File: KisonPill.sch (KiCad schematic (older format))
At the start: 44 parts, among them J1 USB_C_Receptacle_USB2.0, J2 Conn_01x17_Male, J3 Conn_01x17_Male, J4 Conn_01x03_Male, J5 Conn_01x04_Male, J6 Conn_01x03_Male, J7 Conn_01x08_Male, Q1 2N3904S-RTK/PS, Q2 2N3904S-RTK/PS, SW1 SW_Push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

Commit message: save
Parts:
- removed U4: ESP32JtagConnector, KisonCommon:jtag1.27, symbol KisonCommon:ESP32JtagConnector
- added R14, R15: 0, Resistor_SMD:R_0603_1608Metric, symbol Device:R
- added U4: ESP32FullConnector-KisonCommon, KisonCommon:jtag1.27-12, symbol KisonPill-rescue:ESP32FullConnector-KisonCommon
- added U7: ESP32FullConnector, Connector_Molex:Molex_CLIK-Mate_502382-1270_1x12-1MP_P1.25mm_Vertical, symbol KisonPill-rescue:ESP32FullConnector-KisonCommon
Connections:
- net +3V3: now also U4.7 (3V3), U7.7 (3V3)
- net DTR: now also Q2.1 (E); no longer Q2.3 (C)
- net EN: now also U4.1 (TRST), U7.1 (TRST)
- net EXT_5V: now also U4.8 (5V), U7.8 (5V)
- net GND: now also U4.2 (GND), U7.2 (GND)
- net IO0: now also Q2.3 (C), U4.12 (IO0), U7.12 (IO0); no longer Q2.1 (E)
- net IO12: now also U4.3 (TDI), U7.3 (TDI)
- net IO13: now also U4.4 (TCLK), U7.4 (TCLK)
- net IO14: now also U4.5 (TMS), U7.5 (TMS)
- net IO15: now also U4.6 (TDO), U7.6 (TDO); no longer J7.6 (Pin_6)
- net IO32: now also J7.6 (Pin_6)
- net RXD0: now also R14.2, U7.10 (RX)
- net TXD0: now also R15.1, U7.9 (TX)
- new net: R14.1, U4.10 (RX)
- new net: R15.2, U4.9 (TX)
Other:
- note added: "Should we isolate IO0 and rx,tx from Connector to on board?"
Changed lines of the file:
@@
 F 4 "C18536" H 3000 1300 50  0001 C CNN "LCSC"
 	1    3000 1300
-	1    0    0    -1
+	1    0    0    1
 $EndComp
 Wire Wire Line
@@
 Text Label 3100 550  0    50   ~ 0
 EN
-$Comp
-L KisonCommon:ESP32JtagConnector U4
-U 1 1 605BFB02
-P 6750 650
-F 0 "U4" H 6760 775 50  0000 C CNN
-F 1 "ESP32JtagConnector" H 6760 684 50  0000 C CNN
-F 2 "KisonCommon:jtag1.27" H 6750 650 50  0001 C CNN
-F 3 "" H 6750 650 50  0001 C CNN
-	1    6750 650
-	1    0    0    -1
-$EndComp
 $Comp
 L power:+3.3V #PWR012
@@
 Text Label 9250 1600 0    50   ~ 0
 TXD0
-$Comp
-L power:GND #PWR011
-U 1 1 60603F1F
-P 6550 750
-F 0 "#PWR011" H 6550 500 50  0001 C CNN
-F 1 "GND" V 6555 622 50  0000 R CNN
-F 2 "" H 6550 750 50  0001 C CNN
-F 3 "" H 6550 750 50  0001 C CNN
-	1    6550 750
-	0    1    1    0
-$EndComp
-Text Label 7050 750  0    50   ~ 0
+Text Label 5760 910  0    50   ~ 0
 EN
-Wire Wire Line
-	6970 750  7050 750
-Text Label 7050 820  0    50   ~ 0
+Text Label 5760 980  0    50   ~ 0
 IO12
-Wire Wire Line
-	6970 820  7050 820
-Text Label 7050 880  0    50   ~ 0
+Text Label 5760 1050 0    50   ~ 0
 IO14
-Wire Wire Line
-	6970 880  7050 880
-Text Label 6440 820  3    50   ~ 0
-IO13
-Wire Wire Line
-	6440 820  6550 820
-Text Label 6550 880  3    50   ~ 0
-IO15
 $Comp
 L Regulator_Linear:AZ1117-3.3 U3
@@
 Text Label 10220 4300 0    50   ~ 0
 IO4
-Text Label 10220 4400 0    50   ~ 0
-IO15
 Text Label 10220 4500 0    50   ~ 0
 IO5
 Text Label 10220 4600 0    50   ~ 0
 IO35
+Text Label 10220 4400 0    50   ~ 0
+IO32
+$Comp
+L power:+3V3 #PWR0124
+U 1 1 6059C21E
+P 6040 1120
+F 0 "#PWR0124" H 6040 970 50  0001 C CNN
+F 1 "+3V3" H 6055 1293 50  0000 C CNN
+F 2 "" H 6040 1120 50  0001 C CNN
+F 3 "" H 6040 1120 50  0001 C CNN
+	1    6040 1120
+	1    0    0    -1
+$EndComp
+Wire Wire Line
+	6040 1120 5760 1120
+$Comp
+L Device:R R15
+U 1 1 605D512D
+P 5910 1190
+F 0 "R15" V 5910 1190 50  0000 C CNN
+F 1 "0" V 5990 1190 50  0000 C CNN
+F 2 "Resistor_SMD:R_0603_1608Metric" V 5840 1190 50  0001 C CNN
+F 3 "~" H 5910 1190 50  0001 C CNN
+	1    5910 1190
+	0    1    1    0
+$EndComp
+Text Label 6060 1190 0    50   ~ 0
+TXD0
+$Comp
+L KisonPill-rescue:ESP32FullConnector-KisonCommon U7
+U 1 1 605F623D
+P 5750 1880
+F 0 "U7" H 5560 2304 50  0000 C CNN
+F 1 "ESP32FullConnector" H 5560 2213 50  0000 C CNN
+F 2 "Connector_Molex:Molex_CLIK-Mate_502382-1270_1x12-1MP_P1.25mm_Vertical" H 5750 1880 50  0001 C CNN
+F 3 "" H 5750 1880 50  0001 C CNN
+	1    5750 1880
+	1    0    0    -1
+$EndComp
+$Comp
+L power:GND #PWR011
+U 1 1 60603F1F
+P 5120 910
+F 0 "#PWR011" H 5120 660 50  0001 C CNN
+F 1 "GND" V 5125 782 50  0000 R CNN
+F 2 "" H 5120 910 50  0001 C CNN
+F 3 "" H 5120 910 50  0001 C CNN
+	1    5120 910
+	-1   0    0    1
+$EndComp
+Text Label 5340 980  2    50   ~ 0
+IO13
+Text Label 5340 1050 2    50   ~ 0
+IO15
+Wire Wire Line
+	5120 910  5340 910
+Text Label 5340 1120 2    50   ~ 0
+EXT_5V
+Text Label 5340 1260 3    50   ~ 0
+IO0
+$Comp
+L Device:R R14
+U 1 1 605CA1B8
+P 5190 1190
+F 0 "R14" V 5190 1190 50  0000 C CNN
+F 1 "0" V 5270 1190 50  0000 C CNN
+F 2 "Resistor_SMD:R_0603_1608Metric" V 5120 1190 50  0001 C CNN
+F 3 "~" H 5190 1190 50  0001 C CNN
+	1    5190 1190
+	0    1    1    0
+$EndComp
+Text Label 5040 1190 2    50   ~ 0
+RXD0
+$Comp
+L KisonPill-rescue:ESP32FullConnector-KisonCommon U4
+U 1 1 60586A77
+P 5740 1120
+F 0 "U4" H 5550 1544 50  0000 C CNN
+F 1 "ESP32FullConnector-KisonCommon" H 5550 1453 50  0000 C CNN
+F 2 "KisonCommon:jtag1.27-12" H 5740 1120 50  0001 C CNN
+F 3 "" H 5740 1120 50  0001 C CNN
+	1    5740 1120
+	1    0    0    -1
+$EndComp
+$Comp
+L power:GND #PWR09
+U 1 1 6060CCF1
+P 5130 1670
+F 0 "#PWR09" H 5130 1420 50  0001 C CNN
+F 1 "GND" V 5135 1542 50  0000 R CNN
+F 2 "" H 5130 1670 50  0001 C CNN
+F 3 "" H 5130 1670 50  0001 C CNN
+	1    5130 1670
+	-1   0    0    1
+$EndComp
+Text Label 5350 1740 2    50   ~ 0
+IO13
+Text Label 5350 1810 2    50   ~ 0
+IO15
+Wire Wire Line
+	5130 1670 5350 1670
+Text Label 5350 1880 2    50   ~ 0
+EXT_5V
+Text Label 5350 2020 3    50   ~ 0
+IO0
+Text Label 5770 1670 0    50   ~ 0
+EN
+Text Label 5770 1740 0    50   ~ 0
+IO12
+Text Label 5770 1810 0    50   ~ 0
+IO14
+$Comp
+L power:+3V3 #PWR010
+U 1 1 6061353C
+P 6050 1880
+F 0 "#PWR010" H 6050 1730 50  0001 C CNN
+F 1 "+3V3" H 6065 2053 50  0000 C CNN
+F 2 "" H 6050 1880 50  0001 C CNN
+F 3 "" H 6050 1880 50  0001 C CNN
+	1    6050 1880
+	1    0    0    -1
+$EndComp
+Wire Wire Line
+	6050 1880 5770 1880
+Wire Wire Line
+	5350 1950 5040 1950
+Wire Wire Line
+	5040 1950 5040 1190
+Wire Wire Line
+	5770 1950 6170 1950
+Wire Wire Line
+	6170 1950 6170 1190
+Wire Wire Line
+	6170 1190 6060 1190
+Text Notes 4400 610  0    50   ~ 0
+Should we isolate IO0 and rx,tx from Connector to on board?
 $EndSCHEMATC

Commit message: V1
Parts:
- removed C10, C9: 0.1uf, Capacitor_SMD:C_0603_1608Metric, symbol Device:C
- removed C8: 10uf, Capacitor_SMD:C_1206_3216Metric, symbol Device:C
- removed J2, J3: Conn_01x17_Male, Connector_PinHeader_2.54mm:PinHeader_1x17_P2.54mm_Vertical, symbol Connector:Conn_01x17_Male
- removed J4, J6: Conn_01x03_Male, Connector_PinHeader_2.54mm:PinHeader_1x03_P2.54mm_Vertical, symbol Connector:Conn_01x03_Male
- removed J5: Conn_01x04_Male, Connector_PinHeader_2.54mm:PinHeader_1x04_P2.54mm_Vertical, symbol Connector:Conn_01x04_Male
- removed J7: Conn_01x08_Male, Connector_PinHeader_2.54mm:PinHeader_1x08_P2.54mm_Vertical, symbol Connector:Conn_01x08_Male
- removed U5: ICM-20602, Package_LGA:LGA-16_3x3mm_P0.5mm_LayoutBorder3x5y, symbol Sensor_Motion:ICM-20602
- added J2, J3: Conn_01x19_Male, Connector_PinHeader_2.54mm:PinHeader_1x19_P2.54mm_Vertical, symbol Connector:Conn_01x19_Male
- U4, U7: symbol KisonPill-rescue:ESP32FullConnector-KisonCommon -> KisonCommon:ESP32FullConnector
- U6: footprint KisonCommon:USBLC6-2P6 -> KisonCommon:USBLC6-2P6-SOT666
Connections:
- net +3V3: now also J2.1 (Pin_1)
- net CLK: now also J3.19 (Pin_19)
- net CMD: now also J2.18 (Pin_18)
- net EN: now also J2.2 (Pin_2)
- net EXT_5V: now also J2.19 (Pin_19); no longer U4.8 (5V), U7.8 (5V)
- net GND: now also J2.14 (Pin_14), J3.1 (Pin_1), J3.7 (Pin_7)
- net IO0: now also J3.14 (Pin_14)
- net IO12: now also J2.13 (Pin_13)
- net IO13: now also J2.15 (Pin_15)
- net IO14: now also J2.12 (Pin_12)
- net IO15: now also J3.16 (Pin_16)
- net IO16: now also J3.12 (Pin_12)
- net IO17: now also J3.11 (Pin_11)
- net IO18: now also J3.9 (Pin_9)
- net IO19: now also J3.8 (Pin_8)
- net IO2: now also J3.15 (Pin_15)
- net IO21: now also J3.6 (Pin_6)
- net IO22: now also J3.3 (Pin_3)
- net IO23: now also J3.2 (Pin_2)
- net IO25: now also J2.9 (Pin_9)
- net IO26: now also J2.10 (Pin_10)
- net IO27: now also J2.11 (Pin_11)
- net IO32: now also J2.7 (Pin_7)
- net IO33: now also J2.8 (Pin_8)
- net IO34: now also J2.5 (Pin_5)
- net IO35: now also J2.6 (Pin_6)
- net IO4: now also J3.13 (Pin_13)
- net IO5: now also J3.10 (Pin_10)
- net RXD0: now also J3.5 (Pin_5); no longer U7.10 (RX)
- net SD0: now also J3.18 (Pin_18)
- net SD1: now also J3.17 (Pin_17)
- net SD2: now also J2.16 (Pin_16)
- net SD3: now also J2.17 (Pin_17)
- net SENSOR_VN: now also J2.4 (Pin_4)
- net SENSOR_VP: now also J2.3 (Pin_3)
- net TXD0: now also J3.4 (Pin_4); no longer U7.9 (TX)
- net at R14.1, U4.10 (RX): now also U7.10 (RX)
- net at R15.2, U4.9 (TX): now also U7.9 (TX)
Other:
- moved on the sheet: R14, R15

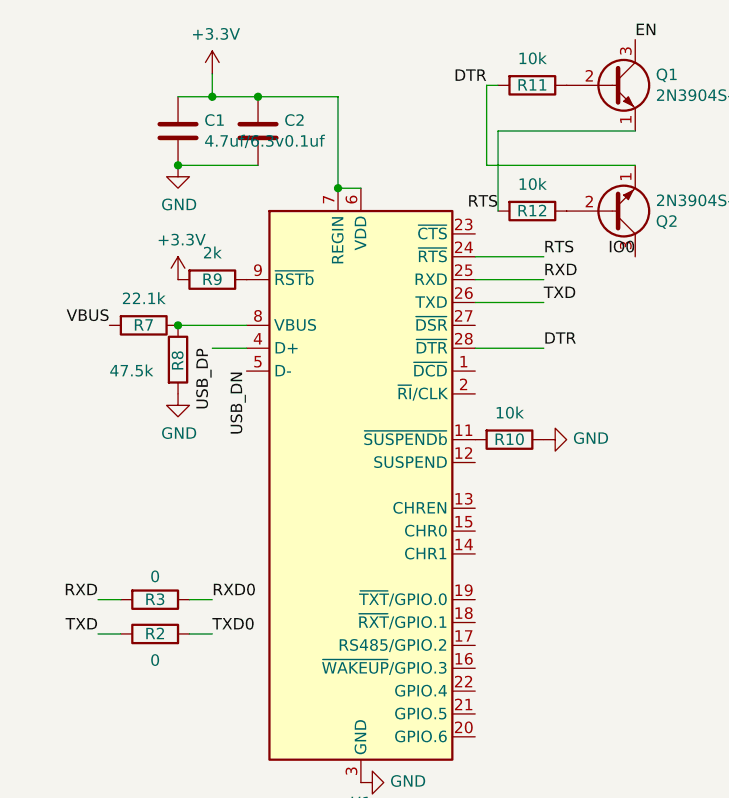
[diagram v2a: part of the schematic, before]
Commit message: Fix Error Over RX&TX
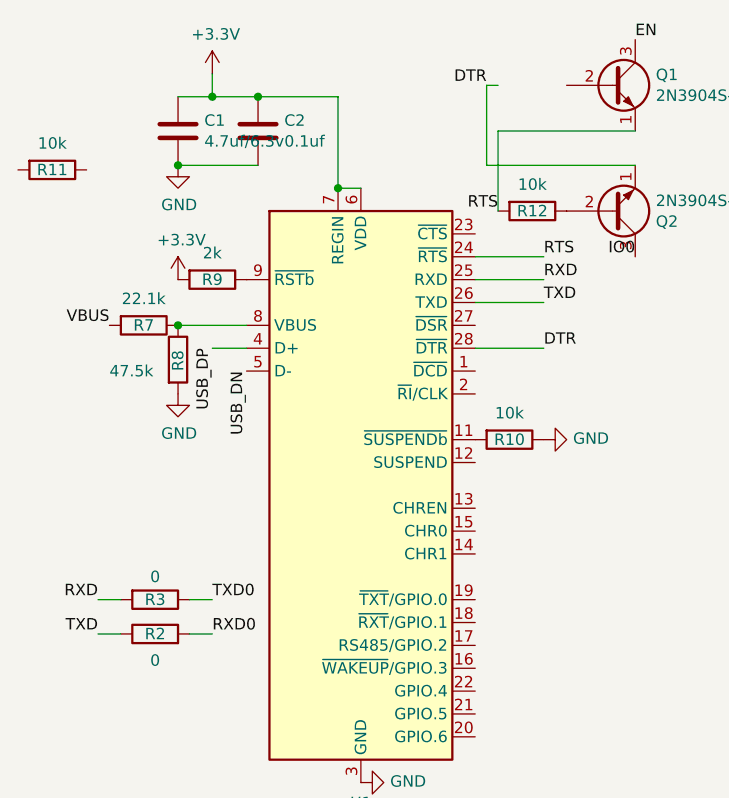
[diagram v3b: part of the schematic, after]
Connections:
- net DTR: no longer R11.2
- net RXD0: now also R2.2; no longer R3.1
- net TXD0: now also R3.1; no longer R2.2
- net at R11.1: no longer Q1.2 (B)
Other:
- moved on the sheet: R11
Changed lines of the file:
@@
 	1800 1200 1900 1200
 Connection ~ 1800 1200
+Text Label 1250 3000 0    50   ~ 0
+TXD0
 Text Label 1250 3150 0    50   ~ 0
-TXD0
-Text Label 1250 3000 0    50   ~ 0
 RXD0
 $Comp
@@
 L Device:R R11
 U 1 1 60593FC3
-P 2650 750
-F 0 "R11" V 2650 750 50  0000 C CNN
-F 1 "10k" V 2534 750 50  0000 C CNN
-F 2 "Resistor_SMD:R_0603_1608Metric" V 2580 750 50  0001 C CNN
-F 3 "~" H 2650 750 50  0001 C CNN
-F 4 "C149898" H 2650 750 50  0001 C CNN "LCSC"
-	1    2650 750
-	0    1    1    0
-$EndComp
+P 550 1120
+F 0 "R11" V 550 1120 50  0000 C CNN
+F 1 "10k" V 434 1120 50  0000 C CNN
+F 2 "Resistor_SMD:R_0603_1608Metric" V 480 1120 50  0001 C CNN
+F 3 "~" H 550 1120 50  0001 C CNN
+F 4 "C149898" H 550 1120 50  0001 C CNN "LCSC"
+	1    550  1120
+	0    1    1    0
+$EndComp
